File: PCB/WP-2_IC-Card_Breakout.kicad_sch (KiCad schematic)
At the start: 3 parts, among them J1 SMS-138-01-G-S, J2 Conn_02x19_Odd_Even_PCB_Edge

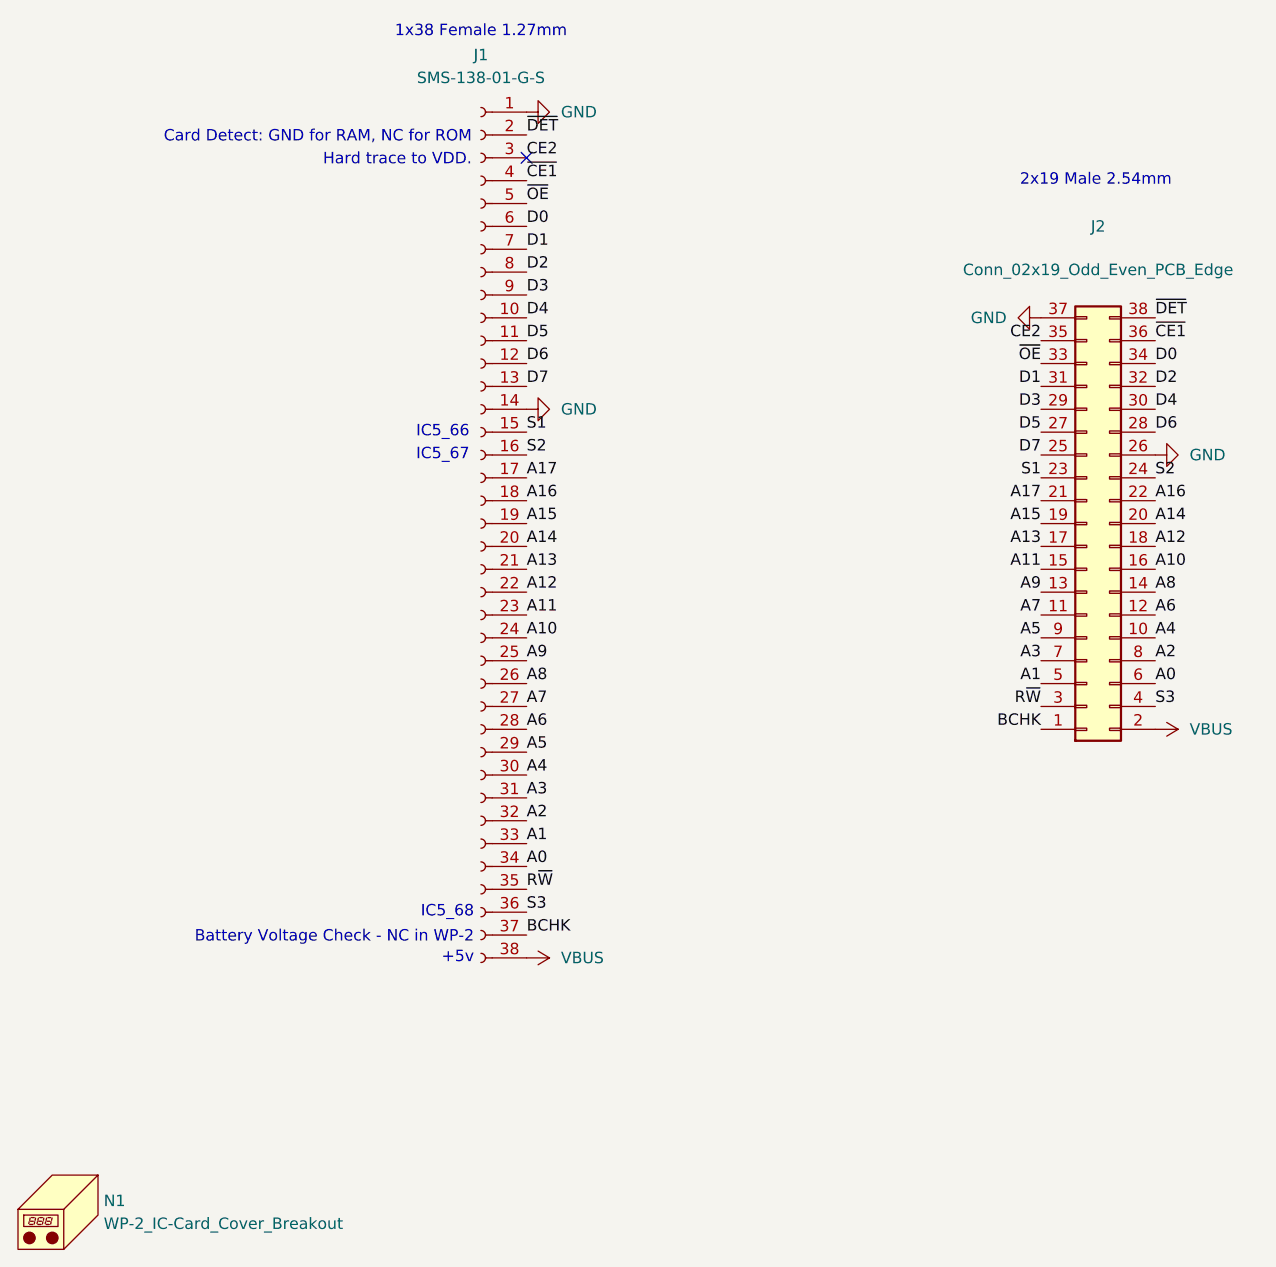
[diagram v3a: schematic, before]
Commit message: sram hand solder D1, breakout T2 trace
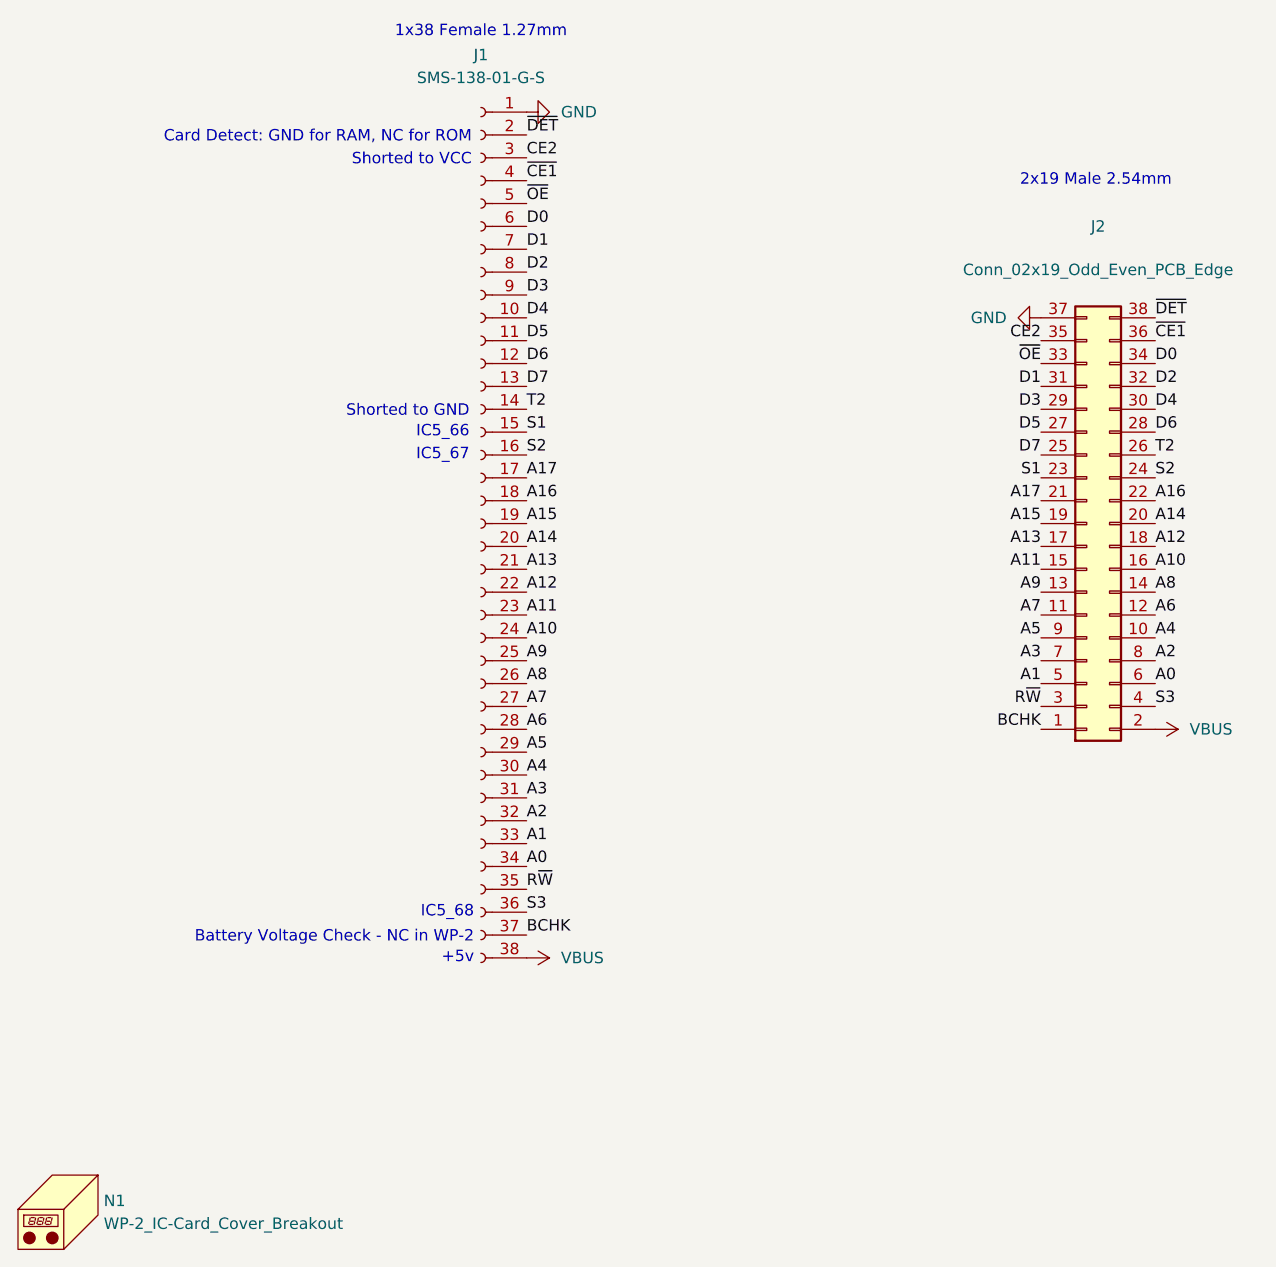
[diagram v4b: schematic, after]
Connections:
- net GND: no longer J1.14 (Pin_14), J2.26 (Pin_26)
- new net T2: J1.14 (Pin_14), J2.26 (Pin_26)
- no-connect marks 1 -> 0
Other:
- note added: "Shorted to GND"
- note added: "Shorted to VCC"
- note removed: "Hard trace to VDD."
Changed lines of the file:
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@@
 		(company "Brian K. White - b.kenyon.w@gmail.com")
 	)
-	(no_connect
-		(at 114.3 60.96)
-	)
 	(text "+5v"
 		(exclude_from_sim no)
@@
 		)
 	)
+	(text "Shorted to GND"
+		(exclude_from_sim no)
+		(at 107.95 89.916 0)
+		(effects
+			(font
+				(size 1.27 1.27)
+			)
+			(justify right bottom)
+		)
+	)
 	(text "Card Detect: GND for RAM, NC for ROM"
 		(exclude_from_sim no)
@@
 		)
 	)
-	(text "Hard trace to VDD."
+	(text "Shorted to VCC"
 		(exclude_from_sim no)
 		(at 108.204 61.976 0)
@@
 		)
 	)
+	(label "T2"
+		(at 184.15 93.98 0)
+		(fields_autoplaced yes)
+		(effects
+			(font
+				(size 1.27 1.27)
+			)
+			(justify left bottom)
+		)
+	)
 	(label "A13"
 		(at 171.45 104.14 180)
@@
 	(label "D4"
 		(at 184.15 88.9 0)
+		(fields_autoplaced yes)
+		(effects
+			(font
+				(size 1.27 1.27)
+			)
+			(justify left bottom)
+		)
+	)
+	(label "T2"
+		(at 114.3 88.9 0)
 		(fields_autoplaced yes)
 		(effects
@@
 	)
 	(symbol
-		(lib_id "power:GND")
-		(at 114.3 88.9 90)
-		(mirror x)
-		(unit 1)
-		(exclude_from_sim no)
-		(in_bom yes)
-		(on_board yes)
-		(dnp no)
-		(property "Reference" "#PWR0108"
-			(at 120.65 88.9 0)
-			(effects
-				(font
-					(size 1.27 1.27)
-				)
-				(hide yes)
-			)
-		)
-		(property "Value" "GND"
-			(at 118.11 88.9 90)
-			(effects
-				(font
-					(size 1.27 1.27)
-				)
-				(justify right)
-			)
-		)
-		(property "Footprint" ""
-			(at 114.3 88.9 0)
-			(effects
-				(font
-					(size 1.27 1.27)
-				)
-				(hide yes)
-			)
-		)
-		(property "Datasheet" ""
-			(at 114.3 88.9 0)
-			(effects
-				(font
-					(size 1.27 1.27)
-				)
-				(hide yes)
-			)
-		)
-		(property "Description" ""
-			(at 114.3 88.9 0)
-			(effects
-				(font
-					(size 1.27 1.27)
-				)
-				(hide yes)
-			)
-		)
-		(pin "1"
-		)
-		(instances
-			(project "WP-2_IC-Card_Breakout"
-				(path "/e6354d08-0260-48e3-9224-e778b3f6e708"
-					(reference "#PWR0108")
-					(unit 1)
-				)
-			)
-		)
-	)
-	(symbol
 		(lib_id "000_LOCAL:Conn_02x19_Odd_Even")
 		(at 177.8 100.33 0)
@@
 					(unit 1)
 				)
-			)
-		)
-	)
-	(symbol
-		(lib_id "power:GND")
-		(at 184.15 93.98 90)
-		(unit 1)
-		(exclude_from_sim no)
-		(in_bom yes)
-		(on_board yes)
-		(dnp no)
-		(property "Reference" "#PWR0106"
-			(at 190.5 93.98 0)
-			(effects
-				(font
-					(size 1.27 1.27)
-				)
-				(hide yes)
-			)
-		)
-		(property "Value" "GND"
-			(at 187.96 93.98 90)
-			(effects
-				(font
-					(size 1.27 1.27)
-				)
-				(justify right)
-			)
-		)
-		(property "Footprint" ""
-			(at 184.15 93.98 0)
-			(effects
-				(font
-					(size 1.27 1.27)
-				)
-				(hide yes)
-			)
-		)
-		(property "Datasheet" ""
-			(at 184.15 93.98 0)
-			(effects
-				(font
-					(size 1.27 1.27)
-				)
-				(hide yes)
-			)
-		)
-		(property "Description" ""
-			(at 184.15 93.98 0)
-			(effects
-				(font
-					(size 1.27 1.27)
-				)
-				(hide yes)
-			)
-		)
-		(pin "1"
-		)
-		(instances
-			(project "WP-2_IC-Card_Breakout"
-				(path "/e6354d08-0260-48e3-9224-e778b3f6e708"
-					(reference "#PWR0106")
-					(unit 1)
-				)

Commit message: update programming adapter & readme
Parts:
- J2: MPN (none) -> PRPC019DAAN-RC
- N1: now left out of the parts list
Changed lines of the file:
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@@
 	(title_block
 		(title "TANDY WP-2 IC Card Breakout")
-		(date "2023-01-01")
-		(rev "003")
+		(date "2025-04-29")
+		(rev "004")
 		(company "Brian K. White - b.kenyon.w@gmail.com")
 	)
@@
 			)
 		)
-		(property "Description" ""
+		(property "Description" "02x19 x 2.54mm pitch male pin header"
+			(at 177.8 100.33 0)
+			(effects
+				(font
+					(size 1.27 1.27)
+				)
+				(hide yes)
+			)
+		)
+		(property "MPN" "PRPC019DAAN-RC"
 			(at 177.8 100.33 0)
 			(effects
@@
 		(unit 1)
 		(exclude_from_sim yes)
-		(in_bom yes)
+		(in_bom no)
 		(on_board yes)
 		(dnp no)

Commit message: silkscreens, board outlines, switch slider, covers fitment, copper to edge
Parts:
- J1: footprint 000_LOCAL:SMS-138-01-x-x_pcb_edge -> 000_LOCAL:SMS-138-01-x-S_pcb_edge
- N1: footprint 000_LOCAL:WP-2_IC_Card_Cover_Breakout -> 000_LOCAL:WP-2_IC-Card_Cover_Breakout
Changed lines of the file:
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@@
 (kicad_sch
-	(version 20231120)
+	(version 20250114)
 	(generator "eeschema")
-	(generator_version "8.0")
+	(generator_version "9.0")
 	(paper "USLetter")
 	(title_block
@@
 	(label "A7"
 		(at 114.3 121.92 0)
-		(fields_autoplaced yes)
 		(effects
 			(font
@@
 	(label "~{DET}"
 		(at 184.15 78.74 0)
-		(fields_autoplaced yes)
 		(effects
 			(font
@@
 	(label "D6"
 		(at 184.15 91.44 0)
-		(fields_autoplaced yes)
 		(effects
 			(font
@@
 	(label "A10"
 		(at 184.15 106.68 0)
-		(fields_autoplaced yes)
 		(effects
 			(font
@@
 	(label "A11"
 		(at 171.45 106.68 180)
-		(fields_autoplaced yes)
 		(effects
 			(font
@@
 	(label "S1"
 		(at 171.45 96.52 180)
-		(fields_autoplaced yes)
 		(effects
 			(font
@@
 	(label "D7"
 		(at 171.45 93.98 180)
-		(fields_autoplaced yes)
 		(effects
 			(font
@@
 	(label "~{CE1}"
 		(at 114.3 63.5 0)
-		(fields_autoplaced yes)
 		(effects
 			(font
@@
 	(label "T2"
 		(at 184.15 93.98 0)
-		(fields_autoplaced yes)
 		(effects
 			(font
@@
 	(label "A13"
 		(at 171.45 104.14 180)
-		(fields_autoplaced yes)
 		(effects
 			(font
@@
 	(label "R~{W}"
 		(at 114.3 142.24 0)
-		(fields_autoplaced yes)
 		(effects
 			(font
@@
 	(label "A8"
 		(at 114.3 119.38 0)
-		(fields_autoplaced yes)
 		(effects
 			(font
@@
 	(label "~{OE}"
 		(at 114.3 66.04 0)
-		(fields_autoplaced yes)
 		(effects
 			(font
@@
 	(label "D3"
 		(at 114.3 76.2 0)
-		(fields_autoplaced yes)
 		(effects
 			(font
@@
 	(label "A6"
 		(at 114.3 124.46 0)
-		(fields_autoplaced yes)
 		(effects
 			(font
@@
 	(label "A12"
 		(at 184.15 104.14 0)
-		(fields_autoplaced yes)
 		(effects
 			(font
@@
 	(label "A13"
 		(at 114.3 106.68 0)
-		(fields_autoplaced yes)
 		(effects
 			(font
@@
 	(label "A15"
 		(at 171.45 101.6 180)
-		(fields_autoplaced yes)
 		(effects
 			(font
@@
 	(label "S2"
 		(at 114.3 93.98 0)
-		(fields_autoplaced yes)
 		(effects
 			(font
@@
 	(label "A12"
 		(at 114.3 109.22 0)
-		(fields_autoplaced yes)
 		(effects
 			(font
@@
 	(label "A10"
 		(at 114.3 114.3 0)
-		(fields_autoplaced yes)
 		(effects
 			(font
@@
 	(label "~{DET}"
 		(at 114.3 58.42 0)
-		(fields_autoplaced yes)
 		(effects
 			(font
@@
 	(label "A8"
 		(at 184.15 109.22 0)
-		(fields_autoplaced yes)
 		(effects
 			(font
@@
 	(label "D6"
 		(at 114.3 83.82 0)
-		(fields_autoplaced yes)
 		(effects
 			(font
@@
 	(label "CE2"
 		(at 171.45 81.28 180)
-		(fields_autoplaced yes)
 		(effects
 			(font
@@
 	(label "A14"
 		(at 114.3 104.14 0)
-		(fields_autoplaced yes)
 		(effects
 			(font
@@
 	(label "D5"
 		(at 171.45 91.44 180)
-		(fields_autoplaced yes)
 		(effects
 			(font
@@
 	(label "S1"
 		(at 114.3 91.44 0)
-		(fields_autoplaced yes)
 		(effects
 			(font
@@
 	(label "A5"
 		(at 171.45 114.3 180)
-		(fields_autoplaced yes)
 		(effects
 			(font
@@
 	(label "D2"
 		(at 184.15 86.36 0)
-		(fields_autoplaced yes)
 		(effects
 			(font
@@
 	(label "A5"
 		(at 114.3 127 0)
-		(fields_autoplaced yes)
 		(effects
 			(font
@@
 	(label "A7"
 		(at 171.45 111.76 180)
-		(fields_autoplaced yes)
 		(effects
 			(font
@@
 	(label "S3"
 		(at 114.3 144.78 0)
-		(fields_autoplaced yes)
 		(effects
 			(font
@@
 	(label "D0"
 		(at 114.3 68.58 0)
-		(fields_autoplaced yes)
 		(effects
 			(font
@@
 	(label "D3"
 		(at 171.45 88.9 180)
-		(fields_autoplaced yes)
 		(effects
 			(font
@@
 	(label "A9"
 		(at 114.3 116.84 0)
-		(fields_autoplaced yes)
 		(effects
 			(font
@@
 	(label "A11"
 		(at 114.3 111.76 0)
-		(fields_autoplaced yes)
 		(effects
 			(font
@@
 	(label "A1"
 		(at 114.3 137.16 0)
-		(fields_autoplaced yes)
 		(effects
 			(font
@@
 	(label "D5"
 		(at 114.3 81.28 0)
-		(fields_autoplaced yes)
 		(effects
 			(font
@@
 	(label "~{OE}"
 		(at 171.45 83.82 180)
-		(fields_autoplaced yes)
 		(effects
 			(font
@@
 	(label "A16"
 		(at 114.3 99.06 0)
-		(fields_autoplaced yes)
 		(effects
 			(font
@@
 	(label "A16"
 		(at 184.15 99.06 0)
-		(fields_autoplaced yes)
 		(effects
 			(font
@@
 	(label "A2"
 		(at 114.3 134.62 0)
-		(fields_autoplaced yes)
 		(effects
 			(font
@@
 	(label "~{CE1}"
 		(at 184.15 81.28 0)
-		(fields_autoplaced yes)
 		(effects
 			(font
@@
 	(label "A0"
 		(at 114.3 139.7 0)
-		(fields_autoplaced yes)
 		(effects
 			(font
@@
 	(label "A2"
 		(at 184.15 116.84 0)
-		(fields_autoplaced yes)
 		(effects
 			(font
@@
 	(label "A14"
 		(at 184.15 101.6 0)
-		(fields_autoplaced yes)
 		(effects
 			(font
@@
 	(label "D1"
 		(at 114.3 71.12 0)
-		(fields_autoplaced yes)
 		(effects
 			(font
@@
 	(label "A3"
 		(at 114.3 132.08 0)
-		(fields_autoplaced yes)
 		(effects
 			(font
@@
 	(label "A15"
 		(at 114.3 101.6 0)
-		(fields_autoplaced yes)
 		(effects
 			(font
@@
 	(label "A9"
 		(at 171.45 109.22 180)
-		(fields_autoplaced yes)
 		(effects
 			(font
@@
 	(label "D7"
 		(at 114.3 86.36 0)
-		(fields_autoplaced yes)
 		(effects
 			(font
@@
 	(label "A6"
 		(at 184.15 111.76 0)
-		(fields_autoplaced yes)
 		(effects
 			(font
@@
 	(label "D2"
 		(at 114.3 73.66 0)
-		(fields_autoplaced yes)
 		(effects
 			(font
@@
 	(label "D1"
 		(at 171.45 86.36 180)
-		(fields_autoplaced yes)
 		(effects
 			(font
@@
 	(label "S3"
 		(at 184.15 121.92 0)
-		(fields_autoplaced yes)
 		(effects
 			(font
@@
 	(label "D4"
 		(at 114.3 78.74 0)
-		(fields_autoplaced yes)
 		(effects
 			(font
@@
 	(label "D0"
 		(at 184.15 83.82 0)
-		(fields_autoplaced yes)
 		(effects
 			(font
@@
 	(label "A4"
 		(at 184.15 114.3 0)
-		(fields_autoplaced yes)
 		(effects
 			(font
@@
 	(label "BCHK"
 		(at 114.3 147.32 0)
-		(fields_autoplaced yes)
 		(effects
 			(font
@@
 	(label "A17"
 		(at 171.45 99.06 180)
-		(fields_autoplaced yes)
 		(effects
 			(font
@@
 	(label "A0"
 		(at 184.15 119.38 0)
-		(fields_autoplaced yes)
 		(effects
 			(font
@@
 	(label "A1"
 		(at 171.45 119.38 180)
-		(fields_autoplaced yes)
 		(effects
 			(font
@@
 	(label "A4"
 		(at 114.3 129.54 0)
-		(fields_autoplaced yes)
 		(effects
 			(font
@@
 	(label "CE2"
 		(at 114.3 60.96 0)
-		(fields_autoplaced yes)
 		(effects
 			(font
@@
 	(label "A3"
 		(at 171.45 116.84 180)
-		(fields_autoplaced yes)
 		(effects
 			(font
@@
 	(label "D4"
 		(at 184.15 88.9 0)
-		(fields_autoplaced yes)
 		(effects
 			(font
@@
 	(label "T2"
 		(at 114.3 88.9 0)
-		(fields_autoplaced yes)
 		(effects
 			(font
@@
 	(label "A17"
 		(at 114.3 96.52 0)
-		(fields_autoplaced yes)
 		(effects
 			(font
@@
 	(label "S2"
 		(at 184.15 96.52 0)
-		(fields_autoplaced yes)
 		(effects
 			(font
@@
 	(label "BCHK"
 		(at 171.45 124.46 180)
-		(fields_autoplaced yes)
 		(effects
 			(font
@@
 	(label "R~{W}"
 		(at 171.45 121.92 180)
-		(fields_autoplaced yes)
 		(effects
 			(font
@@
 			)
 		)
-		(property "Footprint" "000_LOCAL:SMS-138-01-x-x_pcb_edge"
+		(property "Footprint" "000_LOCAL:SMS-138-01-x-S_pcb_edge"
 			(at 109.22 101.6 0)
 			(effects
@@
 			)
 		)
-		(property "Footprint" "000_LOCAL:WP-2_IC_Card_Cover_Breakout"
+		(property "Footprint" "000_LOCAL:WP-2_IC-Card_Cover_Breakout"
 			(at 64.77 176.53 0)
 			(effects
@@
 		)
 	)
+	(embedded_fonts no)
 )

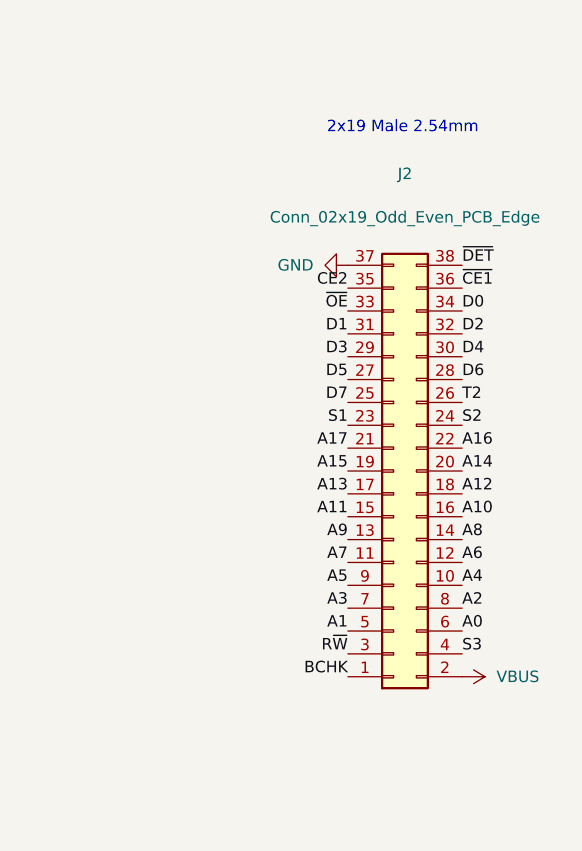
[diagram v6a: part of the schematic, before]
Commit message: breakout pinout
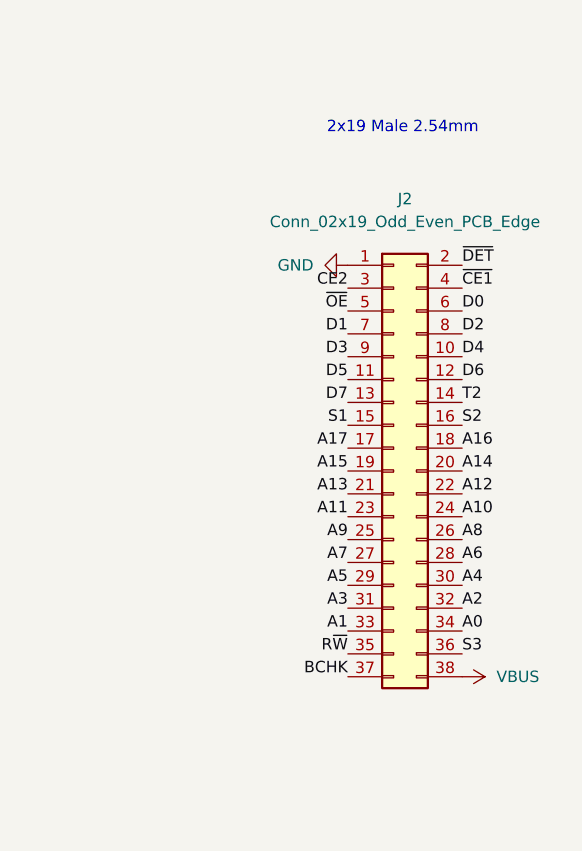
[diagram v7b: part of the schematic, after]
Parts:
- J2: footprint 000_LOCAL:Pin-Header_2x19_P2.54mm_PCB_Edge -> 000_LOCAL:Pin-Header_2x19_P2.54mm_PCB_Edge_L
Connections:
- net A0: now also J2.34 (Pin_34); no longer J2.6 (Pin_6)
- net A1: now also J2.33 (Pin_33); no longer J2.5 (Pin_5)
- net A10: now also J2.24 (Pin_24); no longer J2.16 (Pin_16)
- net A11: now also J2.23 (Pin_23); no longer J2.15 (Pin_15)
- net A12: now also J2.22 (Pin_22); no longer J2.18 (Pin_18)
- net A13: now also J2.21 (Pin_21); no longer J2.17 (Pin_17)
- net A16: now also J2.18 (Pin_18); no longer J2.22 (Pin_22)
- net A17: now also J2.17 (Pin_17); no longer J2.21 (Pin_21)
- net A2: now also J2.32 (Pin_32); no longer J2.8 (Pin_8)
- net A3: now also J2.31 (Pin_31); no longer J2.7 (Pin_7)
- net A4: now also J2.30 (Pin_30); no longer J2.10 (Pin_10)
- net A5: now also J2.29 (Pin_29); no longer J2.9 (Pin_9)
- net A6: now also J2.28 (Pin_28); no longer J2.12 (Pin_12)
- net A7: now also J2.27 (Pin_27); no longer J2.11 (Pin_11)
- net A8: now also J2.26 (Pin_26); no longer J2.14 (Pin_14)
- net A9: now also J2.25 (Pin_25); no longer J2.13 (Pin_13)
- net BCHK: now also J2.37 (Pin_37); no longer J2.1 (Pin_1)
- net CE2: now also J2.3 (Pin_3); no longer J2.35 (Pin_35)
- net D0: now also J2.6 (Pin_6); no longer J2.34 (Pin_34)
- net D1: now also J2.7 (Pin_7); no longer J2.31 (Pin_31)
- net D2: now also J2.8 (Pin_8); no longer J2.32 (Pin_32)
- net D3: now also J2.9 (Pin_9); no longer J2.29 (Pin_29)
- net D4: now also J2.10 (Pin_10); no longer J2.30 (Pin_30)
- net D5: now also J2.11 (Pin_11); no longer J2.27 (Pin_27)
- net D6: now also J2.12 (Pin_12); no longer J2.28 (Pin_28)
- net D7: now also J2.13 (Pin_13); no longer J2.25 (Pin_25)
- net GND: now also J2.1 (Pin_1); no longer J2.37 (Pin_37)
- net R~{W}: now also J2.35 (Pin_35); no longer J2.3 (Pin_3)
- net S1: now also J2.15 (Pin_15); no longer J2.23 (Pin_23)
- net S2: now also J2.16 (Pin_16); no longer J2.24 (Pin_24)
- net S3: now also J2.36 (Pin_36); no longer J2.4 (Pin_4)
- net T2: now also J2.14 (Pin_14); no longer J2.26 (Pin_26)
- net VBUS: now also J2.38 (Pin_38); no longer J2.2 (Pin_2)
- net ~{CE1}: now also J2.4 (Pin_4); no longer J2.36 (Pin_36)
- net ~{DET}: now also J2.2 (Pin_2); no longer J2.38 (Pin_38)
- net ~{OE}: now also J2.5 (Pin_5); no longer J2.33 (Pin_33)
